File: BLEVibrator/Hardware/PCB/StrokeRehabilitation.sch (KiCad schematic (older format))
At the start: 16 parts, among them P1 JST_PH_01x02, P2 CONN_01X05, Q1 MOSFET_N, SW1 SWITCH_DPDT, U1 TPS737, U2 RFD22301, U3 Brushed_DC_motor

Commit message: Updated the PCB to have a side-mounted slide switch and connection status LED. The case still needs to be updated to match
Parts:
- removed C2: 100nF, FabLibrary:C_1206_HandSoldering_IainEdit, symbol C
- removed D1, D2: LED, FabLibrary:C_1206_HandSoldering_IainEdit, symbol LED
- removed SW1: SWITCH_DPDT, IainPersonalLibrary:SlideSwitch_AYZ0202AGRLC, symbol SWITCH_DPDT
- added D1: BI_LED_common_anode, IainPersonalLibrary:Bi_LED_SM1204BC-RG, symbol BI_LED_common_anode
- added SW1: SWITCH_INV, IainPersonalLibrary:SlideSwitch_SSSS810701, symbol SWITCH_INV
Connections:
- wire segments 63 -> 58
- no-connect marks 8 -> 5
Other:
- moved on the sheet: R2
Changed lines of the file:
@@
 LIBS:contrib
 LIBS:valves
+LIBS:FabLibrary
 LIBS:IainPersonalLibrary
 LIBS:StrokeRehabilitation-cache
@@
 $EndComp
 $Comp
-L LED D1
-U 1 1 56CB0BBE
-P 6700 3000
-F 0 "D1" H 6700 3100 50  0000 C CNN
-F 1 "LED" H 6700 2900 50  0000 C CNN
-F 2 "FabLibrary:C_1206_HandSoldering_IainEdit" H 6700 3000 50  0001 C CNN
-F 3 "" H 6700 3000 50  0000 C CNN
-	1    6700 3000
-	0    -1   -1   0
-$EndComp
-$Comp
-L LED D2
-U 1 1 56CB0C01
-P 7000 3000
-F 0 "D2" H 7000 3100 50  0000 C CNN
-F 1 "LED" H 7000 2900 50  0000 C CNN
-F 2 "FabLibrary:C_1206_HandSoldering_IainEdit" H 7000 3000 50  0001 C CNN
-F 3 "" H 7000 3000 50  0000 C CNN
-	1    7000 3000
-	0    -1   -1   0
-$EndComp
-$Comp
 L R R2
 U 1 1 56CB0C84
-P 7000 3450
-F 0 "R2" V 7080 3450 50  0000 C CNN
-F 1 "500" V 7000 3450 50  0000 C CNN
-F 2 "FabLibrary:C_1206_HandSoldering_IainEdit" V 6930 3450 50  0001 C CNN
-F 3 "" H 7000 3450 50  0000 C CNN
-	1    7000 3450
+P 6900 3450
+F 0 "R2" V 6980 3450 50  0000 C CNN
+F 1 "500" V 6900 3450 50  0000 C CNN
+F 2 "FabLibrary:C_1206_HandSoldering_IainEdit" V 6830 3450 50  0001 C CNN
+F 3 "" H 6900 3450 50  0000 C CNN
+	1    6900 3450
 	1    0    0    -1
 $EndComp
@@
 $EndComp
 $Comp
-L C C2
-U 1 1 56CB195F
-P 4300 3950
-F 0 "C2" H 4325 4050 50  0000 L CNN
-F 1 "100nF" H 4325 3850 50  0000 L CNN
-F 2 "FabLibrary:C_1206_HandSoldering_IainEdit" H 4338 3800 50  0001 C CNN
-F 3 "" H 4300 3950 50  0000 C CNN
-	1    4300 3950
-	0    1    1    0
-$EndComp
-$Comp
 L VDD #PWR07
 U 1 1 56CB1B18
@@
 L VDD #PWR010
 U 1 1 56CB3133
-P 6850 2500
-F 0 "#PWR010" H 6850 2350 50  0001 C CNN
-F 1 "VDD" H 6850 2650 50  0000 C CNN
-F 2 "" H 6850 2500 50  0000 C CNN
-F 3 "" H 6850 2500 50  0000 C CNN
-	1    6850 2500
+P 6800 2350
+F 0 "#PWR010" H 6800 2200 50  0001 C CNN
+F 1 "VDD" H 6800 2500 50  0000 C CNN
+F 2 "" H 6800 2350 50  0000 C CNN
+F 3 "" H 6800 2350 50  0000 C CNN
+	1    6800 2350
 	1    0    0    -1
 $EndComp
@@
 Connection ~ 1300 1300
 Wire Wire Line
-	1600 1300 1600 2400
-Connection ~ 1600 1300
-Wire Wire Line
 	4450 1050 4450 1350
 Wire Wire Line
@@
 Connection ~ 4200 3850
 Wire Wire Line
-	4600 3950 4450 3950
-Wire Wire Line
-	4150 3950 3950 3950
+	3950 3950 4600 3950
 Wire Wire Line
 	4600 4150 4150 4150
@@
 Connection ~ 6250 4450
 Wire Wire Line
-	6850 2500 6850 2600
-Wire Wire Line
-	6700 2600 7000 2600
-Wire Wire Line
-	6700 2600 6700 2800
-Wire Wire Line
-	7000 2600 7000 2800
-Connection ~ 6850 2600
-Wire Wire Line
-	6700 3200 6700 3300
-Wire Wire Line
-	7000 3200 7000 3300
+	6700 3150 6700 3300
+Wire Wire Line
+	6900 3150 6900 3300
 Wire Wire Line
 	1150 1550 1150 1400
 Wire Wire Line
-	7000 3600 7000 4250
+	6900 3600 6900 4250
 Wire Wire Line
 	6700 3600 6700 4150
@@
 	6700 4150 6200 4150
 Wire Wire Line
-	7000 4250 6200 4250
+	6900 4250 6200 4250
 Wire Wire Line
 	9300 1950 10150 1950
@@
 	9300 2750 10150 2750
 Connection ~ 9750 2750
-$Comp
-L SWITCH_DPDT SW1
-U 1 1 56C7419A
-P 2250 2300
-F 0 "SW1" H 2250 2750 70  0000 C CNN
-F 1 "SWITCH_DPDT" H 2250 1850 70  0000 C CNN
-F 2 "IainPersonalLibrary:SlideSwitch_AYZ0202AGRLC" H 2250 2300 60  0001 C CNN
-F 3 "" H 2250 2300 60  0000 C CNN
-	1    2250 2300
-	-1   0    0    -1
-$EndComp
-Wire Wire Line
-	1600 2400 1750 2400
-Wire Wire Line
-	1750 2600 1700 2600
-Wire Wire Line
-	1700 2600 1700 1400
-Connection ~ 1700 1400
-Wire Wire Line
-	2750 2500 2950 2500
-NoConn ~ 1750 2000
-NoConn ~ 1750 2200
-NoConn ~ 2750 2100
 $Comp
 L TPS737 U1
@@
 $EndComp
 Wire Wire Line
-	2950 2500 2950 1600
-Wire Wire Line
 	2950 1600 3100 1600
 Wire Wire Line
@@
 Wire Wire Line
 	1150 1300 3100 1300
+$Comp
+L SWITCH_INV SW1
+U 1 1 5755A76A
+P 2200 2200
+F 0 "SW1" H 2000 2350 50  0000 C CNN
+F 1 "SWITCH_INV" H 2050 2050 50  0000 C CNN
+F 2 "IainPersonalLibrary:SlideSwitch_SSSS810701" H 2200 2200 50  0001 C CNN
+F 3 "" H 2200 2200 50  0000 C CNN
+	1    2200 2200
+	-1   0    0    1
+$EndComp
+Wire Wire Line
+	2950 1600 2950 2200
+Wire Wire Line
+	2950 2200 2700 2200
+Wire Wire Line
+	1700 2300 1600 2300
+Wire Wire Line
+	1600 2300 1600 1400
+Connection ~ 1600 1400
+Wire Wire Line
+	1700 2100 1700 1300
+Connection ~ 1700 1300
+$Comp
+L BI_LED_common_anode D1
+U 1 1 5755BF9A
+P 6800 2850
+F 0 "D1" H 7100 2950 50  0000 C CNN
+F 1 "BI_LED_common_anode" H 6910 2610 50  0001 C CNN
+F 2 "IainPersonalLibrary:Bi_LED_SM1204BC-RG" H 6800 2850 60  0001 C CNN
+F 3 "" H 6800 2850 60  0000 C CNN
+	1    6800 2850
+	0    -1   -1   0
+$EndComp
+Wire Wire Line
+	6800 2350 6800 2500
 $EndSCHEMATC

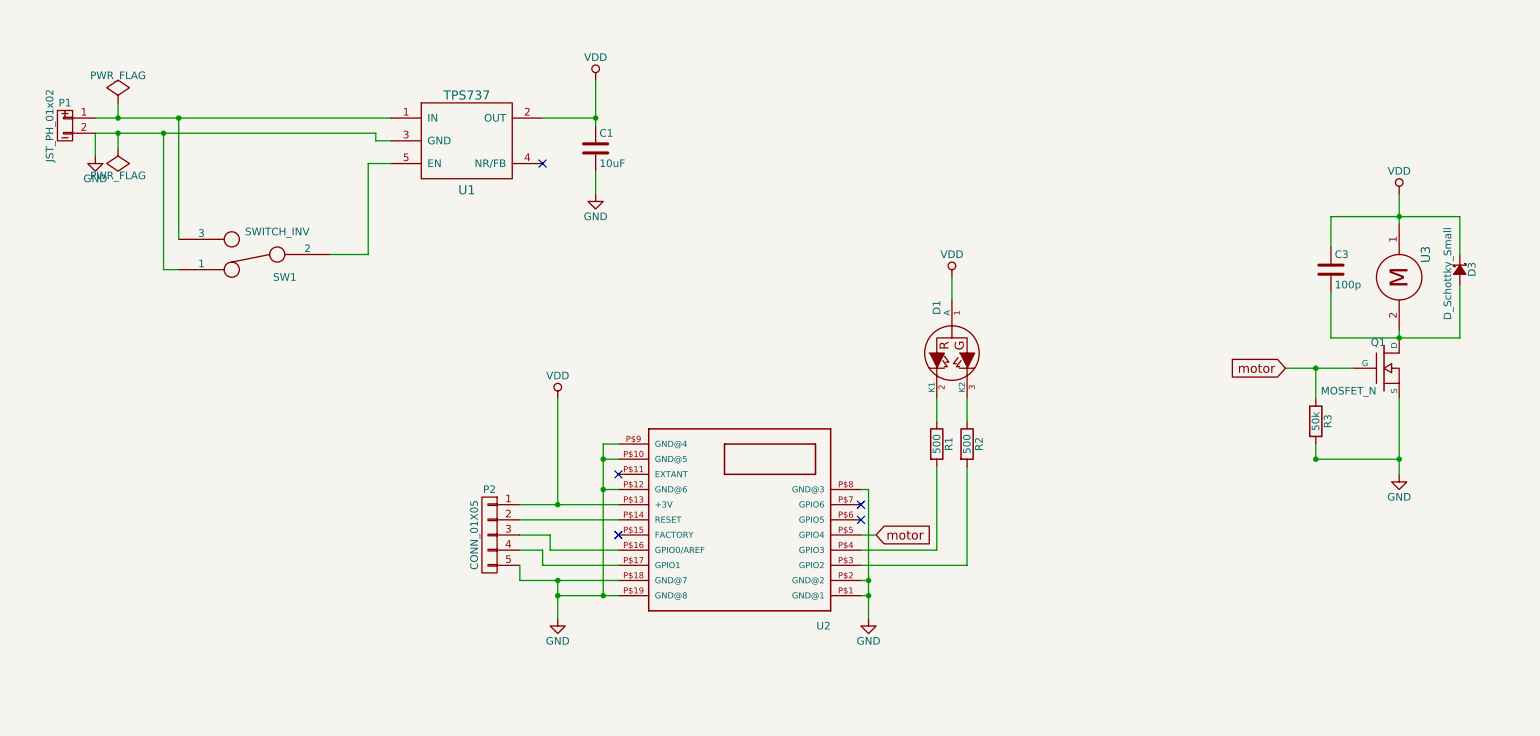
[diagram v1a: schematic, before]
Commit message: Updated schematic and netlist to include lipo charging with a micro USB header
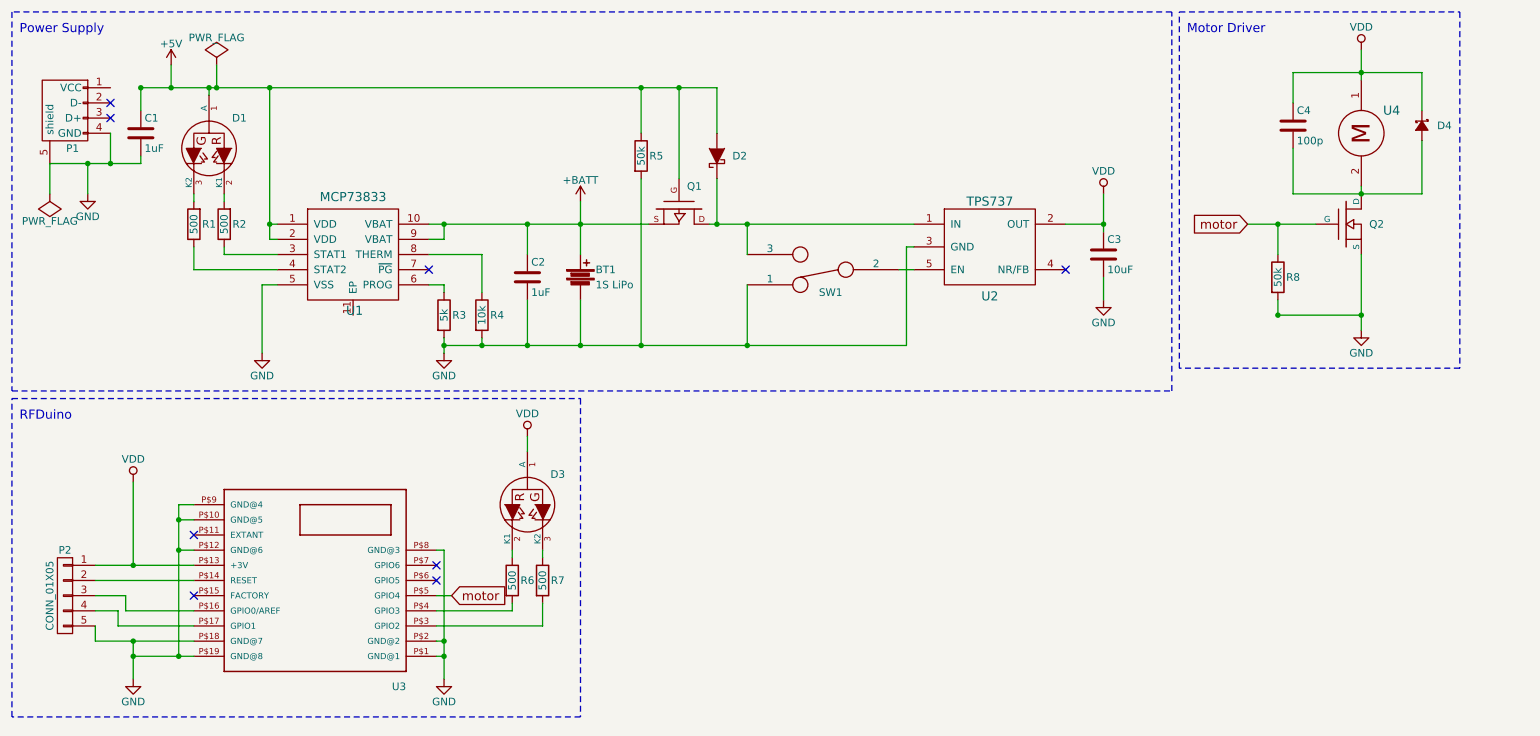
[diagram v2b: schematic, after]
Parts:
- removed P1: JST_PH_01x02, IainPersonalLibrary:S2B_PH_SM4_TB, symbol JST_PH_01x02
- added BT1: 1S LiPo, symbol Battery
- added C1, C2: 1uF, FabLibrary:C_1206_HandSoldering_IainEdit, symbol C
- added D1: BI_LED_common_anode, IainPersonalLibrary:Bi_LED_SM1204BC-RG, symbol BI_LED_common_anode
- added D2: D_Schottky, symbol D_Schottky
- added P1: USB_A, symbol USB_A
- added Q1: MOS_P, symbol MOS_P
- added R1, R2: 500, FabLibrary:C_1206_HandSoldering_IainEdit, symbol R
- added R3: 5k, FabLibrary:C_1206_HandSoldering_IainEdit, symbol R
- added R4: 10k, FabLibrary:C_1206_HandSoldering_IainEdit, symbol R
- added R5: 50k, FabLibrary:C_1206_HandSoldering_IainEdit, symbol R
- added U1: MCP73833, symbol MCP73833
- renumbered C1 to C3, C3 to C4, D1 to D3, D3 to D4, Q1 to Q2, R1 to R6, R2 to R7, R3 to R8, U1 to U2, U2 to U3, U3 to U4
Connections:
- net GND: now also BT1.2, C1.2, C2.2, P1.4 (GND), P1.5 (shield), R3.2, R4.2, R5.2, U1.5 (VSS)
- net at SW1.3, U2.1 (IN): now also D2.1 (K), Q1.D
- new net: R2.1, U1.3 (STAT1)
- new net: R1.1, U1.4 (STAT2)
- new net: R3.1, U1.6 (PROG)
- new net: R4.1, U1.8 (THERM)
- new net: D1.2 (K1), R2.2
- new net: D1.3 (K2), R1.2
- new net +5V: C1.1, D1.1 (A), D2.2 (A), Q1.G, R5.1, U1.1 (VDD), U1.2 (VDD)
- new net +BATT: BT1.1, C2.1, Q1.S, U1.10 (VBAT), U1.9 (VBAT)
- no-connect marks 5 -> 8
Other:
- note added: "Motor Driver"
- note added: "Power Supply"
- note added: "RFDuino"
- moved on the sheet: C3, C4, D3, D4, P2, Q2, R6, R7, R8, SW1, U2, U3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

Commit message: Cleaned up schematic. Fixed symbols to have pins for matching footprints e.g. exposed thermal pads. Changed LED resistors from 500 to 330 (closer to 4 mA per pin limit of RFDuino, and still within 20 mA limit of the LEDs when on 5V from USB). Created necessary footprints and reasigned to 0805 size as standard.
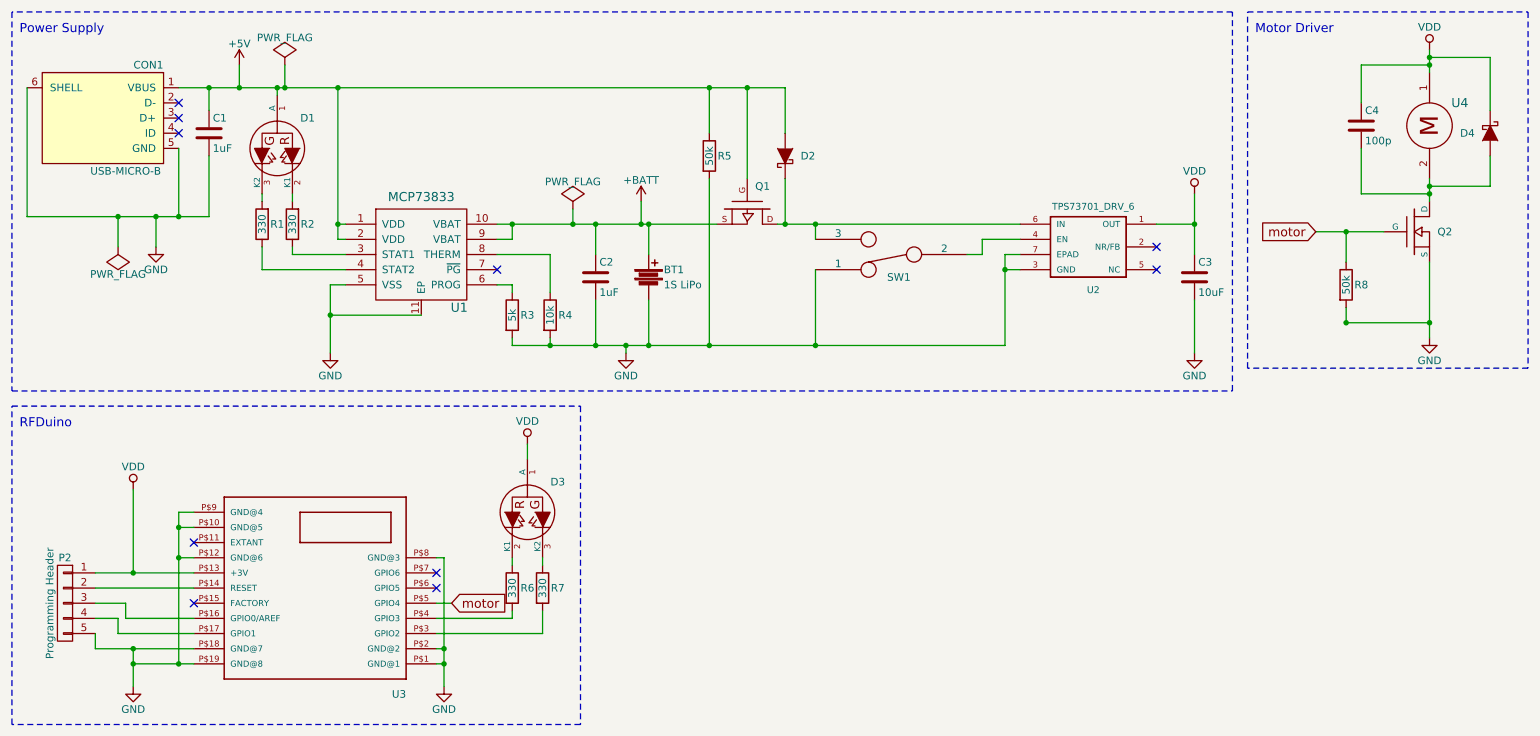
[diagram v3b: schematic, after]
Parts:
- removed D4: D_Schottky_Small, IainPersonalLibrary:SOD-123_a, symbol D_Schottky_Small
- removed P1: USB_A, symbol USB_A
- removed U2: TPS737, IainPersonalLibrary:SOT-223-5, symbol TPS737
- added CON1: USB-MICRO-B, IainPersonalLibrary:Micro_USB_Amphenol_10118192-0001LF, symbol USB-MICRO-B
- added D4: D_Schottky, IainPersonalLibrary:SOD-123F, symbol D_Schottky
- added U2: TPS73701_DRV_6, IainPersonalLibrary:TPS73701_DRV_6, symbol TPS73701_DRV_6
- BT1: footprint (none) -> Wire_Connections_Bridges:WireConnection_0.80mmDrill
- C1, C2, C3, C4: footprint FabLibrary:C_1206_HandSoldering_IainEdit -> IainPersonalLibrary:Murata_capacitor_SMD_0805_reflow
- D2: footprint (none) -> IainPersonalLibrary:SOD-123F
- P2: value CONN_01X05 -> Programming Header
- Q1: footprint (none) -> IainPersonalLibrary:Vishay_SOT-23
- R1, R2, R6, R7: value 500 -> 330; footprint FabLibrary:C_1206_HandSoldering_IainEdit -> IainPersonalLibrary:Yageo_resistor_SMD_0805_reflow
- R3, R4, R5, R8: footprint FabLibrary:C_1206_HandSoldering_IainEdit -> IainPersonalLibrary:Yageo_resistor_SMD_0805_reflow
- U1: footprint (none) -> IainPersonalLibrary:MCP73833-XXX_MF
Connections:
- net +5V: now also CON1.1 (VBUS)
- net GND: now also U1.11 (EP), CON1.5 (GND), CON1.6 (SHELL), U2.3 (GND), U2.7 (EPAD)
- net VDD: now also D4.1 (K), U2.1 (OUT)
- net at C4.2, Q2.D, U4.2: now also D4.2 (A)
- net at D2.1 (K), Q1.D, SW1.3: now also U2.6 (IN)
- net at SW1.2: now also U2.4 (EN)
- no-connect marks 8 -> 10
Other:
- moved on the sheet: BT1, C1, C2, C3, C4, D1, D2, D3, P2, Q1, Q2, R1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

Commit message: Routed the new PCB. Assigned correct footprints in schematic
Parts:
- BT1: footprint Wire_Connections_Bridges:WireConnection_0.80mmDrill -> IainPersonalLibrary:BatteryCon_WireSolder_0.8mm
- U4: footprint IainPersonalLibrary:PrecisionMicrodrives_304_111_Connector_long -> IainPersonalLibrary:WireToBoard_1x2_TensionRelief
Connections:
- net VDD: now also U4.2; no longer U4.1
- net at C4.2, D4.2 (A), Q2.D: now also U4.1; no longer U4.2
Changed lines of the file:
@@
 F 0 "U4" V 10100 1150 60  0000 C CNN
 F 1 "Brushed_DC_motor" H 9950 1600 60  0001 C CNN
-F 2 "IainPersonalLibrary:PrecisionMicrodrives_304_111_Connector_long" H 9950 1350 60  0001 C CNN
+F 2 "IainPersonalLibrary:WireToBoard_1x2_TensionRelief" H 9950 1350 60  0001 C CNN
 F 3 "" H 9950 1350 60  0000 C CNN
 	1    9950 1350
-	0    -1   -1   0
+	0    1    1    0
 $EndComp
 $Comp
@@
 F 0 "BT1" H 4900 2400 50  0000 L CNN
 F 1 "1S LiPo" H 4900 2300 50  0000 L CNN
-F 2 "Wire_Connections_Bridges:WireConnection_0.80mmDrill" V 4800 2390 50  0001 C CNN
+F 2 "IainPersonalLibrary:BatteryCon_WireSolder_0.8mm" V 4800 2390 50  0001 C CNN
 F 3 "" V 4800 2390 50  0000 C CNN
 	1    4800 2350
@@
 $EndComp
 Wire Wire Line
-	9950 2250 9950 2750
+	9950 2250 9950 2650
+Wire Wire Line
+	9950 2650 9950 2750
 Wire Wire Line
 	9400 2550 9400 2650
@@
 Connection ~ 9400 2650
 Wire Wire Line
-	9200 2050 9650 2050
+	9200 2050 9400 2050
+Wire Wire Line
+	9400 2050 9650 2050
 Wire Wire Line
 	9400 2050 9400 2250
@@
 	1400 3750 1400 4300
 Wire Wire Line
-	1150 4300 1800 4300
+	1150 4300 1400 4300
+Wire Wire Line
+	1400 4300 1800 4300
 Connection ~ 1400 4300
 Wire Wire Line
@@
 	1150 4700 1150 4800
 Wire Wire Line
-	1150 4800 1800 4800
-Wire Wire Line
-	1400 4900 1800 4900
-Wire Wire Line
-	1400 4800 1400 5050
+	1150 4800 1400 4800
+Wire Wire Line
+	1400 4800 1800 4800
+Wire Wire Line
+	1400 4900 1700 4900
+Wire Wire Line
+	1700 4900 1800 4900
+Wire Wire Line
+	1400 4800 1400 4900
+Wire Wire Line
+	1400 4900 1400 5050
 Connection ~ 1400 4900
 Connection ~ 1400 4800
@@
 	1800 3900 1700 3900
 Wire Wire Line
-	1700 3900 1700 4900
+	1700 3900 1700 4000
+Wire Wire Line
+	1700 4000 1700 4200
+Wire Wire Line
+	1700 4200 1700 4900
 Wire Wire Line
 	1700 4000 1800 4000
@@
 	3400 4200 3450 4200
 Wire Wire Line
-	3450 4200 3450 5050
+	3450 4200 3450 4800
+Wire Wire Line
+	3450 4800 3450 4900
+Wire Wire Line
+	3450 4900 3450 5050
 Wire Wire Line
 	3400 4800 3450 4800
@@
 	4000 3450 4000 3550
 Wire Wire Line
-	700  1950 1900 1950
+	700  1950 1300 1950
+Wire Wire Line
+	1300 1950 1550 1950
+Wire Wire Line
+	1550 1950 1700 1950
+Wire Wire Line
+	1700 1950 1900 1950
 Wire Wire Line
 	1550 1950 1550 2150
@@
 	2800 2400 2700 2400
 Wire Wire Line
-	2700 2400 2700 2850
+	2700 2400 2700 2600
+Wire Wire Line
+	2700 2600 2700 2850
 Wire Wire Line
 	2100 1100 2100 950
@@
 Connection ~ 4150 2800
 Wire Wire Line
-	3800 2000 5250 2000
+	3800 2000 3900 2000
+Wire Wire Line
+	3900 2000 4300 2000
+Wire Wire Line
+	4300 2000 4450 2000
+Wire Wire Line
+	4450 2000 4750 2000
+Wire Wire Line
+	4750 2000 4800 2000
+Wire Wire Line
+	4800 2000 5250 2000
 Wire Wire Line
 	4800 2800 4800 2500
 Wire Wire Line
-	2750 1100 2750 2100
+	2750 1100 2750 2000
+Wire Wire Line
+	2750 2000 2750 2100
 Wire Wire Line
 	2800 2200 2450 2200
@@
 Connection ~ 5450 1100
 Wire Wire Line
-	5650 2000 7250 2000
+	5650 2000 5700 2000
+Wire Wire Line
+	5700 2000 5900 2000
+Wire Wire Line
+	5900 2000 7250 2000
 Wire Wire Line
 	5200 1100 5200 1400
@@
 	4100 4550 4100 4700
 Wire Wire Line
-	8400 1800 8400 2200
+	8400 1800 8400 2000
+Wire Wire Line
+	8400 2000 8400 2200
 Wire Wire Line
 	5900 2100 5900 2000
@@
 Connection ~ 4750 2000
 Wire Wire Line
-	9950 850  9950 1000
-Wire Wire Line
-	9950 1700 9950 1850
+	9950 850  9950 900
+Wire Wire Line
+	9950 900  9950 950
+Wire Wire Line
+	9950 950  9950 1000
+Wire Wire Line
+	9950 1700 9950 1750
+Wire Wire Line
+	9950 1750 9950 1800
+Wire Wire Line
+	9950 1800 9950 1850
 Wire Wire Line
 	9950 950  9500 950
@@
 $EndComp
 Wire Wire Line
-	7150 2800 7150 2200
+	7150 2800 7150 2300
+Wire Wire Line
+	7150 2300 7150 2200
 Wire Wire Line
 	7150 2200 7250 2200
@@
 	7000 2100 7250 2100
 Wire Wire Line
-	3900 2800 7150 2800
+	3900 2800 4150 2800
+Wire Wire Line
+	4150 2800 4450 2800
+Wire Wire Line
+	4450 2800 4650 2800
+Wire Wire Line
+	4650 2800 4800 2800
+Wire Wire Line
+	4800 2800 5200 2800
+Wire Wire Line
+	5200 2800 5900 2800
+Wire Wire Line
+	5900 2800 7150 2800
 Wire Wire Line
 	3900 2800 3900 2750
@@
 Connection ~ 1300 1950
 Wire Wire Line
-	1700 1100 5700 1100
+	1700 1100 1900 1100
+Wire Wire Line
+	1900 1100 2100 1100
+Wire Wire Line
+	2100 1100 2350 1100
+Wire Wire Line
+	2350 1100 2400 1100
+Wire Wire Line
+	2400 1100 2750 1100
+Wire Wire Line
+	2750 1100 5200 1100
+Wire Wire Line
+	5200 1100 5450 1100
+Wire Wire Line
+	5450 1100 5700 1100
 Wire Wire Line
 	1900 1250 1900 1100
@@
 	4300 1900 4300 2000
 Connection ~ 4300 2000
+Wire Wire Line
+	9950 1000 9950 1000
+Wire Wire Line
+	9950 1700 9950 1700
 $EndSCHEMATC
